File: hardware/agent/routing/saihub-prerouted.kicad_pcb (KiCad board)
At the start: 2 copper layers, 48 x 28 mm, 55 parts, among them J1 USB4105-GF-A, J2 1x12 2.54mm right-angle, Q1 AO3400A, SW1 BOOT, U1 USBLC6-2SC6, U2 SGM6232YPS8G/TR, U3 ESPC5-32E-H4, U4 TPS2553DBVR, U5 TPS2553DBVR

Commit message: feat(hardware): add header protection and refresh board deliverables
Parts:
- removed R13, R14: 10k, Saihub:R_0603_1608Metric
- added C21: 100n, Saihub:C_0603_1608Metric, F.Cu at (6.00, 4.30)
- added U10: USBLC6-2SC6, Saihub:SOT-23-6, F.Cu at (2.50, 5.50)
- added U6: TPD4E05U06DQAR, Saihub:TPD4E05U06_DQA, F.Cu at (14.5, 4.30)
- added U7: TPD4E05U06DQAR, Saihub:TPD4E05U06_DQA, F.Cu at (22.2, 4.30)
- D3: value SS14 -> SS34
- R10, R12, R9: value 100k -> 10k
- U4, U5: value TPS2553DBVR -> TPS2553DDBVR
- moved Q1 18.0 mm to (2.50, 25.5)
- moved R6 11.2 mm to (2.50, 15.8)
- moved C6 3.30 mm to (2.50, 8.80), turned to 0 degrees
- moved R11 2.36 mm to (15.3, 27.0)
- moved R12 2.05 mm to (22.0, 27.0), turned to 0 degrees
- moved U3 1.95 mm to (14.5, 15.6)
- moved TP3 1.90 mm to (5.60, 27.0)
- moved TP4 1.90 mm to (7.80, 27.0)
- moved TP5 1.90 mm to (10.0, 27.0)
- moved TP6 1.90 mm to (12.2, 27.0)
- moved C13 1.80 mm to (18.5, 27.0)
- moved C8 1.70 mm to (2.50, 14.1), turned to 0 degrees
- moved C7 1.70 mm to (2.50, 10.7), turned to 0 degrees
- moved TP1 0.80 mm to (1.20, 22.3)
- moved TP2 0.80 mm to (3.40, 22.3)
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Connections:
- U3 pad 19: (no net) -> FAULT4
- U3 pad 5: (no net) -> FAULT5
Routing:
- net V5: track 13.8 -> 49.8 mm, vias 1 -> 4
- net VBUS: track 0.00 -> 9.55 mm, vias 0 -> 2
- net V3V3: track 9.59 -> 16.1 mm, vias 1 -> 3
- net GND: track 3.81 -> 8.61 mm, vias 11 -> 17
- net MCU_DP: track 3.19 -> 5.72 mm
- net MCU_DM: track 4.30 -> 6.25 mm

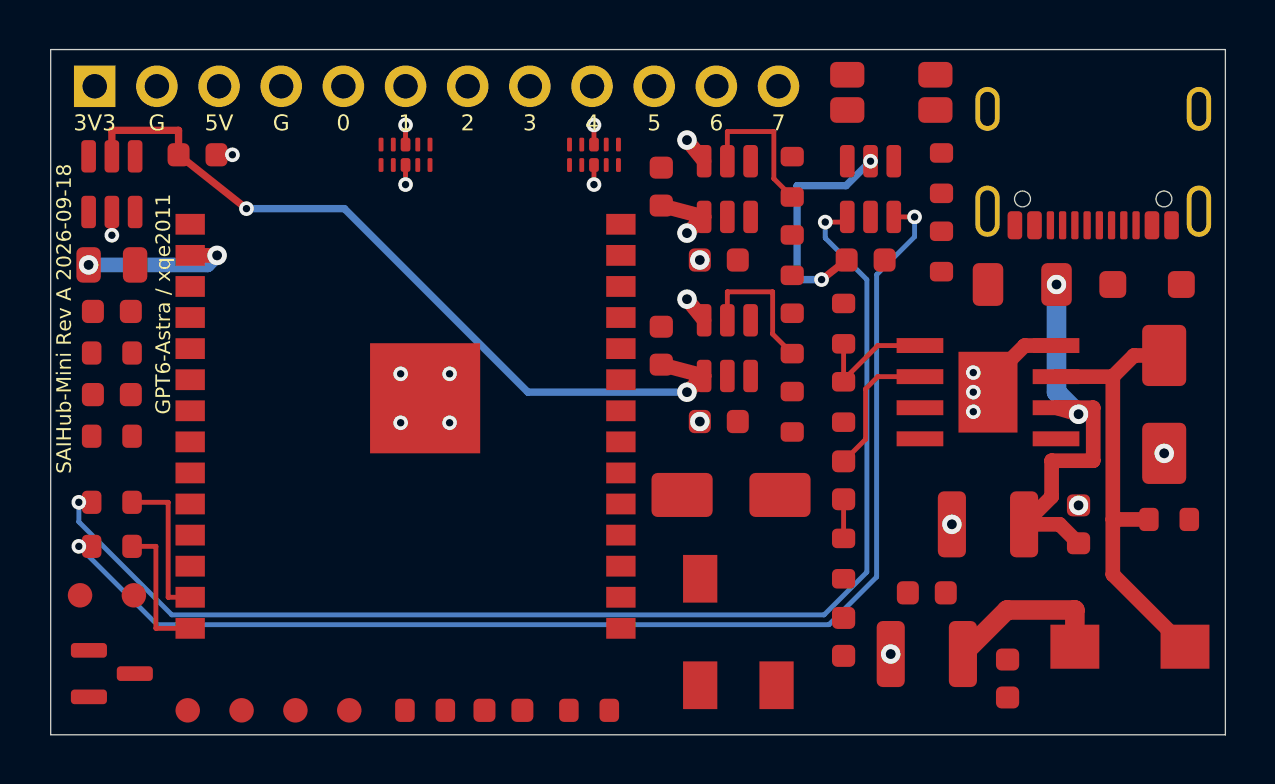
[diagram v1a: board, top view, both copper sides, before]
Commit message: Replace button and add corner antenna module without enlarging PCB
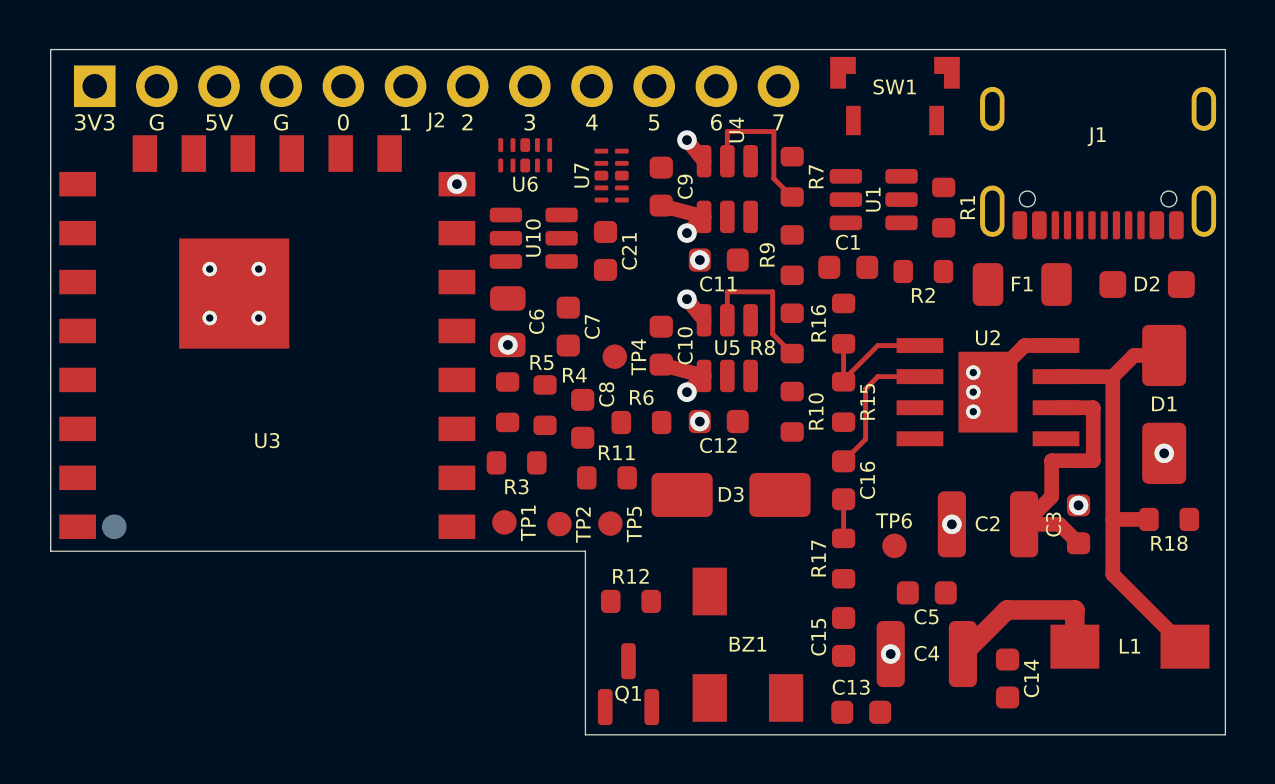
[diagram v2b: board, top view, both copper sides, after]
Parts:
- SW1: footprint Saihub:SW_SPST_EVQP7A -> Saihub:SW_SPST_TS2435VS
- TP3: moved to B.Cu
- U3: value ESPC5-32E-H4 -> ESPC5-12-H4; footprint Saihub:ESPC5-32E-H4 -> Saihub:ESPC5-12-H4
- moved TP6 23.3 mm to (34.5, 20.3)
- moved R6 21.6 mm to (24.1, 15.2), turned to 180 degrees
- moved Q1 21.1 mm to (23.6, 25.9), turned to 90 degrees
- moved TP4 21.0 mm to (23.1, 12.6)
- moved C8 19.3 mm to (21.7, 15.1), turned to 90 degrees
- moved C7 18.7 mm to (21.1, 11.3), turned to 90 degrees
- moved R4 18.6 mm to (20.2, 14.5), turned to 90 degrees
- moved TP2 17.6 mm to (20.8, 19.4)
- moved TP1 17.6 mm to (18.5, 19.3)
- moved U10 17.4 mm to (19.7, 7.71), turned to 180 degrees
- moved C21 17.1 mm to (22.7, 8.23), turned to 90 degrees
- moved R3 16.6 mm to (19.0, 16.9), turned to 180 degrees
- moved C6 16.3 mm to (18.7, 11.1), turned to 90 degrees
- moved R5 16.3 mm to (18.7, 14.4), turned to 90 degrees
- moved TP5 15.0 mm to (22.9, 19.4)
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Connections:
- U3 pad 1: GND -> IO2
- U3 pad 15: BOOT -> GND
- U3 pad 16: IO5 -> IO6
- U3 pad 17: IO4 -> FAULT4
- U3 pad 18: (no net) -> BOOT
- U3 pad 19: FAULT4 -> (no net)
- U3 pad 2: V3V3 -> IO1
- U3 pad 21: IO3 -> BUZZ_PWM
- U3 pad 22: (no net) -> UART_TX
- U3 pad 23: IO7 -> GND
- U3 pad 4: (no net) -> IO3
- U3 pad 6: IO2 -> IO4
- U3 pad 7: IO1 -> IO5
- U3 pad 8: IO6 -> V3V3
- U3 pad 9: (no net) -> IO7
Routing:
- net USB_DM: track 51.8 -> 0.00 mm, vias 2 -> 0
- net USB_DP: track 51.5 -> 0.00 mm, vias 2 -> 0
- net V5: track 49.8 -> 13.8 mm, vias 4 -> 1
- net VBUS: track 9.55 -> 0.00 mm, vias 2 -> 0
- net V3V3: track 16.1 -> 9.59 mm
- net MCU_DM: track 6.25 -> 0.00 mm
- net MCU_DP: track 5.72 -> 0.00 mm
- net GND: track 8.61 -> 3.81 mm, vias 17 -> 11
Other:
- outline, holes or cut-outs redrawn
- board text added: "SAIHub-Mini Rev A 2026-09-24"
- board text removed: "SAIHub-Mini Rev A 2026-09-18"
